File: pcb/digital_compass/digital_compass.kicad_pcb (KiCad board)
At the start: 2 copper layers, 66 x 66 mm, 10 parts, among them SW1 SW_SPDT, U1 L7805, U2 Seeed Studio XIAO SAMD21, U3 Level_Shifter, U4 QMC5883L, U5 Adafruit_Neopixel_Ring_24

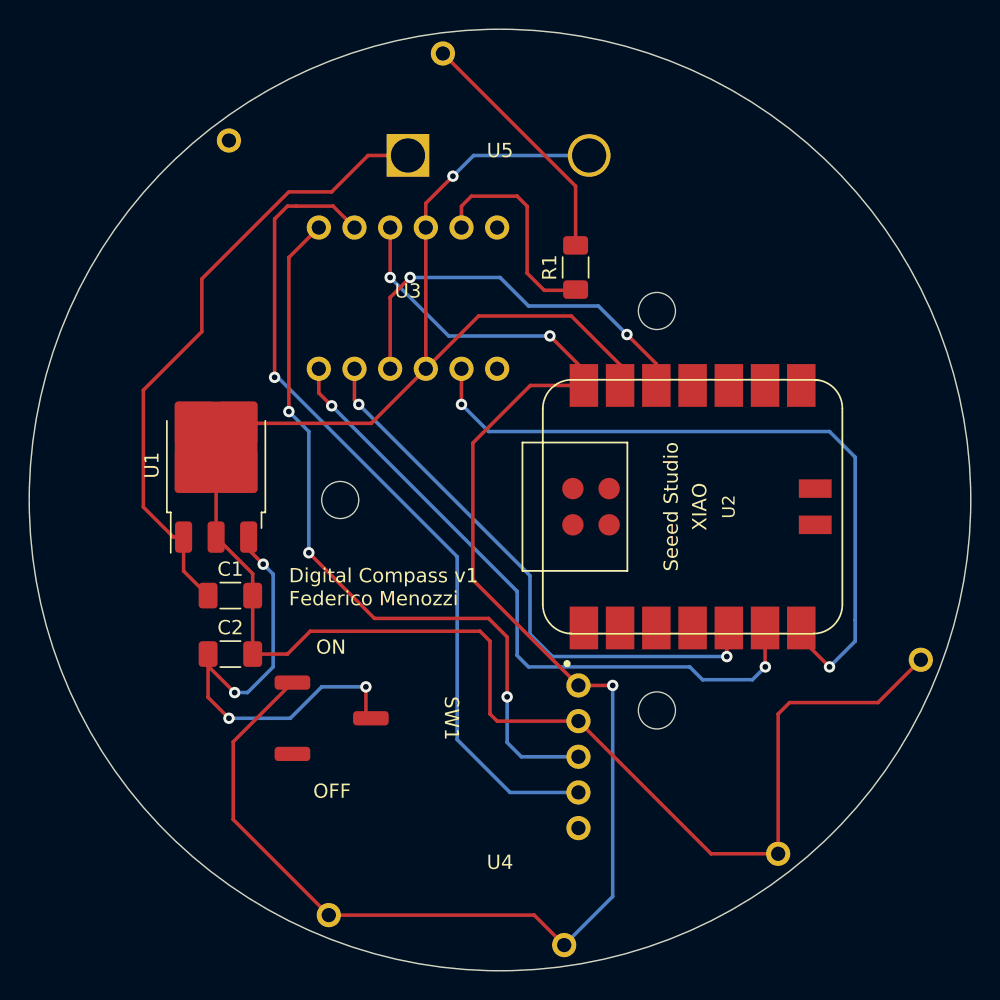
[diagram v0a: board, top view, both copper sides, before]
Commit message: Fix magnetometer and update schematic/pcb/gerbers.
Turns out the original v1 magnetometer footprint had the pins in reverse
order, so update the footprint/schematic/pcb/gerbers for round two at
jlcpcb.
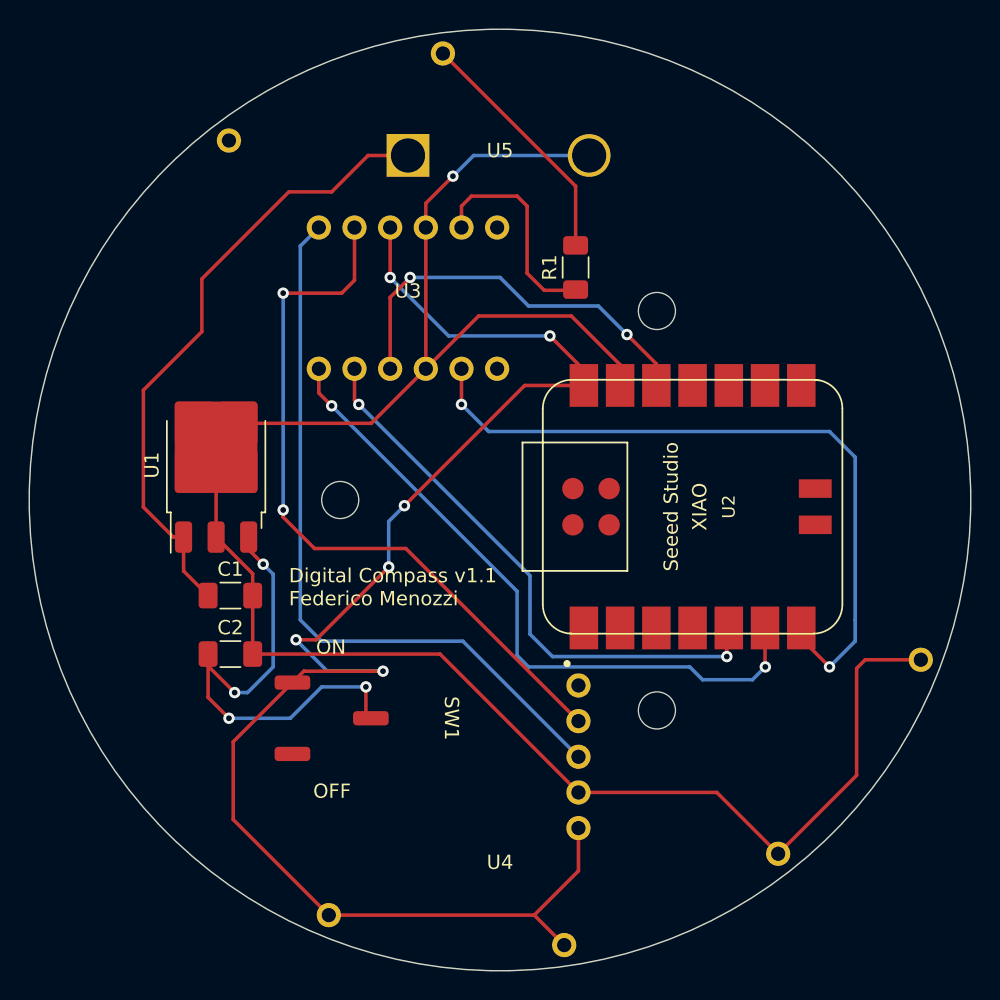
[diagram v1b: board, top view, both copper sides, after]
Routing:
- net Net-(U3-HV2): track 58.6 -> 51.4 mm, vias 1 -> 2
- net GND: track 141.1 -> 135.4 mm
- net Net-(U3-HV1): track 53.4 -> 51.5 mm, vias 3 -> 0
- net Net-(SW1-A): track 110.5 -> 109.5 mm, vias 3 -> 6
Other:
- board text added: "Digital Compass v1.1 Federico Menozzi"
- board text removed: "Digital Compass v1 Federico Menozzi"

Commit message: Fix power switch and update schematic/pcb/gerbers.
Turns out the L7805 consumes power when connected to an input power
source even if the output is disconnected. We therefore move the power
switch to the input side of the regulator to prevent power consumption
when the compass is turned off.
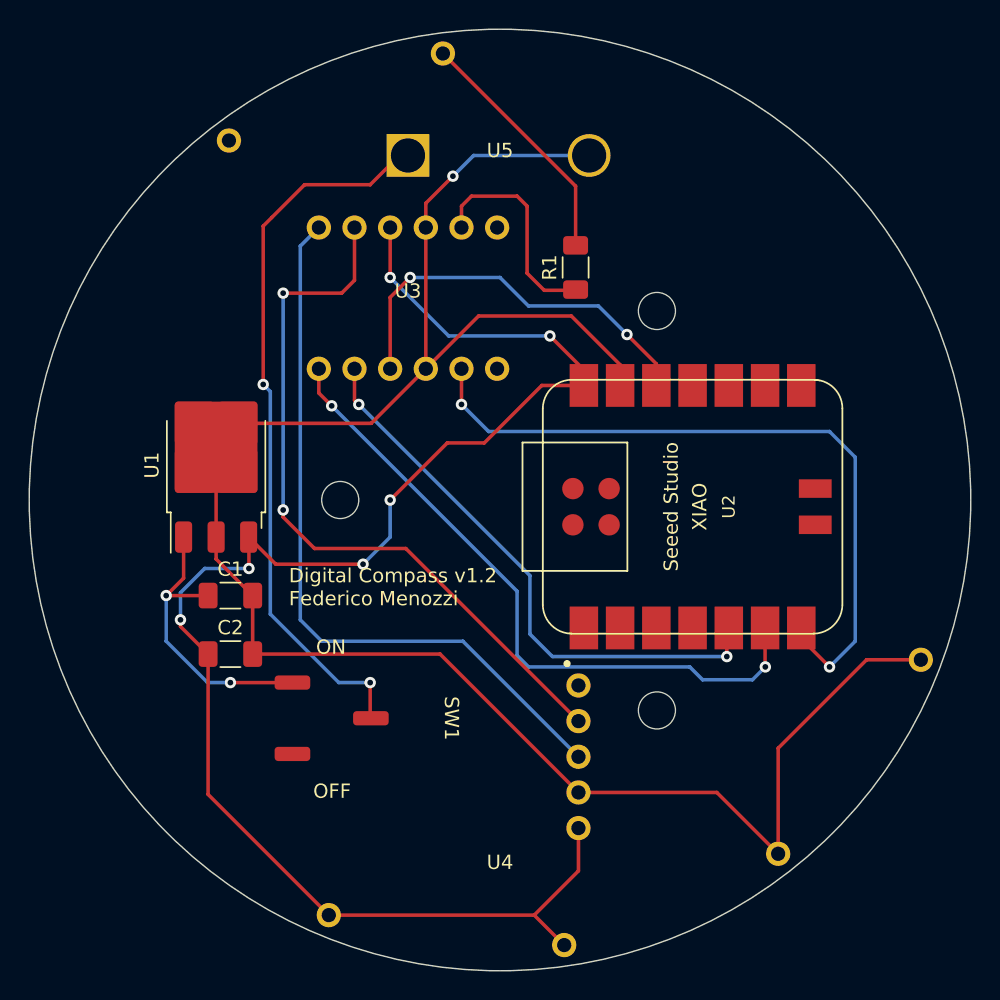
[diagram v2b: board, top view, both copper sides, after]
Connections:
- C1 pad 1: +9V -> Net-(SW1-A)
- C2 pad 1: Net-(SW1-B) -> Net-(U1-OUT)
- SW1 pad 2: Net-(SW1-B) -> +9V
- U1 pad 1: +9V -> Net-(SW1-A)
- U1 pad 3: Net-(SW1-B) -> Net-(U1-OUT)
- U2 pad 14: Net-(SW1-A) -> Net-(U1-OUT)
- U3 pad 10: Net-(SW1-A) -> Net-(U1-OUT)
- U4 pad 1: Net-(SW1-A) -> Net-(U1-OUT)
- U5 pad 1: Net-(SW1-A) -> Net-(U1-OUT)
- U5 pad 2: Net-(SW1-A) -> Net-(U1-OUT)
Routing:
- net Net-(U1-OUT): track 0.00 -> 111.2 mm, vias 0 -> 6
- net Net-(SW1-A): track 109.5 -> 20.8 mm, vias 6 -> 2
- net Net-(SW1-B): track 34.7 -> 0.00 mm, vias 4 -> 0
- net +9V: track 44.2 -> 51.1 mm, vias 0 -> 2
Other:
- board text added: "Digital Compass v1.2 Federico Menozzi"
- board text removed: "Digital Compass v1.1 Federico Menozzi"
